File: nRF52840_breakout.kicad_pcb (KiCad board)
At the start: 4 copper layers, 24.1 x 34.3 mm, 66 parts, among them J2 Conn_ARM_JTAG_SWD_10, J3 Conn_01x22, J4 Conn_01x16, J5 Conn_01x22, J6 S2B-PH-SM4-TB(LF)(SN), J7 Conn_Coaxial, U1 nRF52840, U2 BQ24072, U3 TPS63031, U4 BME680, U5 MM8130-2600RA2, Y1 SiT1533, Y2 32MHz-XRCGB32M000F1H00R0

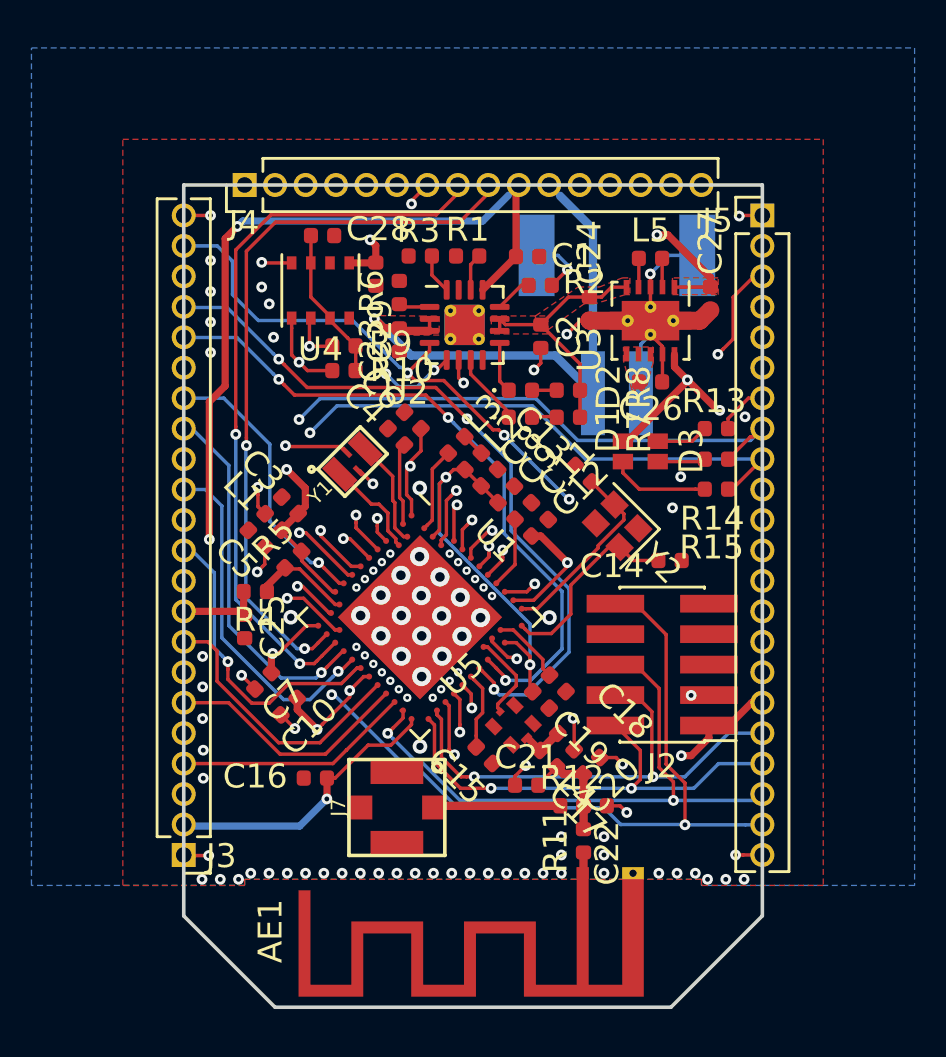
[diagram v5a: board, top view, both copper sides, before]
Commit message: 2 layer som version
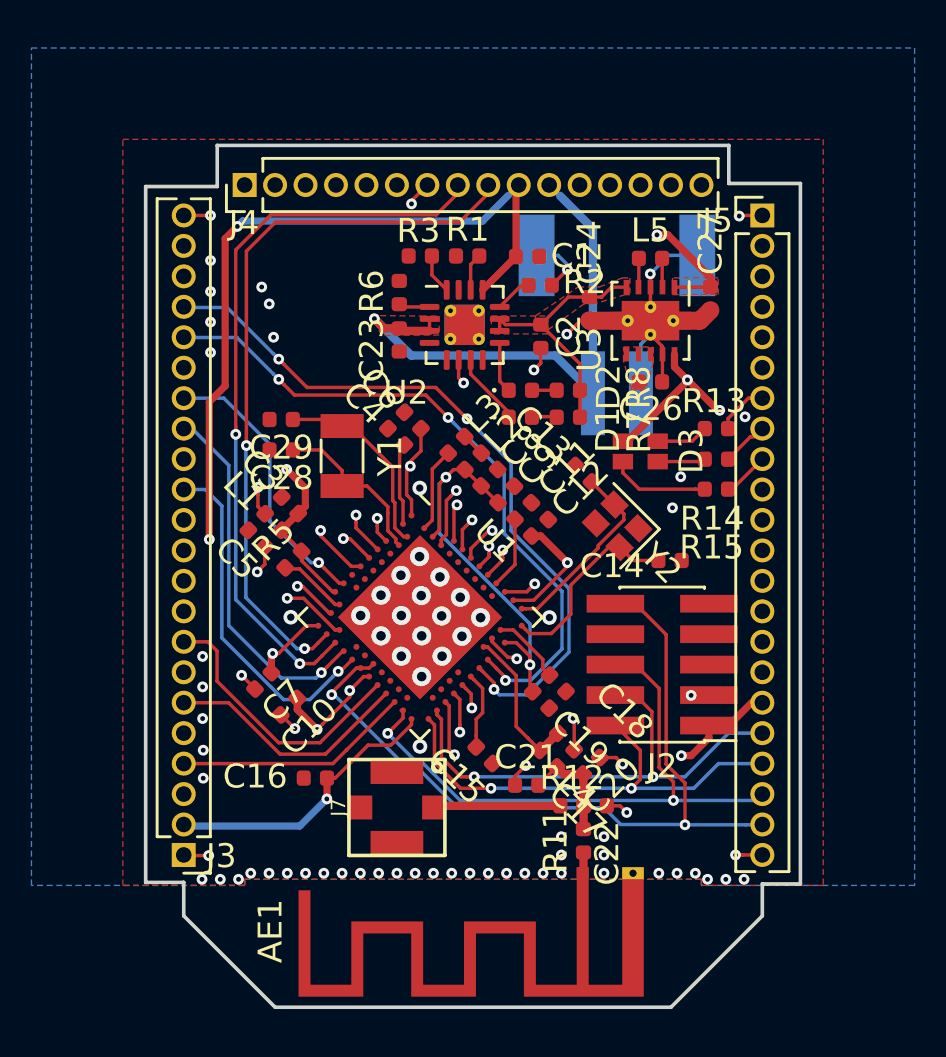
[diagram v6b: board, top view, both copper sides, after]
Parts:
- removed C25: NC, Capacitor_SMD:C_0402_1005Metric
- removed R10, R9: 4.7k, Resistor_SMD:R_0402_1005Metric
- removed R4: NC, Resistor_SMD:R_0402_1005Metric
- removed U4: BME680, Package_LGA:Bosch_LGA-8_3x3mm_P0.8mm_ClockwisePinNumbering
- removed U5: MM8130-2600RA2, custom_footprints:MM8930_2620
- AE1: value Antenna_Shield -> TI_SWRA117D
- C28, C29: value 100nF -> 12.5pF
- J7: value Conn_Coaxial -> U.FL_A-1JB
- L1: value NC -> 10uF
- R13, R14, R15: value 1.5k -> 180R
- Y1: value SiT1533 -> 32.768kHz; footprint custom_footprints:Crystal_SMD_2012-4Pin_2.2mmx1.4mm -> Crystal:Crystal_SMD_3215-2Pin_3.2x1.5mm
- moved C28 9.10 mm to (103.1, 64.4)
- moved C29 7.23 mm to (103.1, 63.1), turned to 180 degrees
- moved Y1 0.49 mm to (105.7, 64.6), turned to 270 degrees
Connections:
- C28 pad 1: GND -> Net-(C28-Pad1)
- C28 pad 2: VDDIO -> GND
- C29 pad 1: GND -> Net-(C29-Pad1)
- C29 pad 2: VDD_nRF -> GND
- J3 pad 10: P0.19 -> Net-(J3-Pad10)
- J3 pad 11: P0.17 -> Net-(J3-Pad11)
- J3 pad 12: P0.16 -> Net-(J3-Pad12)
- J3 pad 14: P0.14 -> Net-(J3-Pad14)
- J3 pad 17: P0.11 -> Net-(J3-Pad17)
- J3 pad 21: P0.03_AIN1 -> Net-(J3-Pad21)
- J3 pad 3: P0.25 -> Net-(J3-Pad3)
- J3 pad 5: P0.23 -> Net-(J3-Pad5)
- J3 pad 7: P0.21 -> Net-(J3-Pad7)
- J3 pad 9: VDDH -> Net-(J3-Pad9)
- J4 pad 1: P0.07 -> Net-(J4-Pad1)
- J4 pad 13: P0.30_AIN6 -> Net-(J4-Pad13)
- J4 pad 15: P0.28_AIN4 -> Net-(J4-Pad15)
- J4 pad 3: P0.05_AIN3 -> Net-(J4-Pad3)
- J4 pad 5: P0.27 -> Net-(J4-Pad5)
- J5 pad 10: P1.07 -> Net-(J5-Pad10)
- J5 pad 12: P1.05 -> Net-(J5-Pad12)
- J5 pad 14: P1.03 -> Net-(J5-Pad14)
- J5 pad 16: P1.01 -> Net-(J5-Pad16)
- J5 pad 3: P1.14 -> Net-(J5-Pad3)
- J5 pad 5: P1.12 -> Net-(J5-Pad5)
- J5 pad 6: P1.11 -> Net-(J5-Pad6)
- J5 pad 9: P1.08 -> Net-(J5-Pad9)
- U1 pad AC11: P0.16 -> Net-(U1-PadAC11)
- U1 pad AC15: P0.19 -> Net-(U1-PadAC15)
- U1 pad AC17: P0.21 -> Net-(U1-PadAC17)
- U1 pad AC19: P0.23 -> Net-(U1-PadAC19)
- U1 pad AC21: P0.25 -> Net-(U1-PadAC21)
- U1 pad AC9: P0.14 -> Net-(U1-PadAC9)
- U1 pad AD12: P0.17 -> P1.18_RESET
- U1 pad B11: P0.28_AIN4 -> Net-(U1-PadB11)
- U1 pad B13: P0.03_AIN1 -> Net-(U1-PadB13)
- U1 pad B15: P1.14 -> Net-(U1-PadB15)
- U1 pad B17: P1.12 -> Net-(U1-PadB17)
- U1 pad B19: P1.11 -> Net-(U1-PadB19)
- U1 pad B9: P0.30_AIN6 -> Net-(U1-PadB9)
- U1 pad D2: Net-(U1-PadD2) -> Net-(C29-Pad1)
- U1 pad F2: Net-(U1-PadF2) -> Net-(C28-Pad1)
- U1 pad H2: P0.27 -> Net-(U1-PadH2)
- U1 pad H23: Net-(U1-PadH23) -> Net-(C17-Pad2)
- U1 pad K2: P0.05_AIN3 -> Net-(U1-PadK2)
- U1 pad M2: P0.07 -> Net-(U1-PadM2)
- U1 pad P2: P1.08 -> Net-(U1-PadP2)
- U1 pad P23: P1.07 -> Net-(U1-PadP23)
- U1 pad T2: P0.11 -> Net-(U1-PadT2)
- U1 pad T23: P1.05 -> Net-(U1-PadT23)
- U1 pad V23: P1.03 -> Net-(U1-PadV23)
- U1 pad Y23: P1.01 -> Net-(U1-PadY23)
- Y1 pad 1: Net-(U1-PadF2) -> Net-(C28-Pad1)
- Y1 pad 2: GND -> Net-(C29-Pad1)
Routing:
- net P1.09: track 35.1 -> 1.47 mm, vias 3 -> 0
- net P1.08: track 34.5 -> 1.48 mm, vias 3 -> 0
- net P0.03_AIN1: track 28.2 -> 0.00 mm, vias 4 -> 0
- net P0.28_AIN4: track 19.7 -> 0.00 mm, vias 1 -> 0
- net P0.27: track 19.3 -> 0.00 mm, vias 3 -> 0
- net P0.07: track 18.3 -> 0.00 mm, vias 1 -> 0
- net P1.14: track 18.2 -> 0.00 mm, vias 2 -> 0
- net P0.30_AIN6: track 17.8 -> 0.00 mm, vias 1 -> 0
- net P1.01: track 17.8 -> 0.00 mm, vias 1 -> 0
- net P1.05: track 17.4 -> 0.00 mm, vias 1 -> 0
- net P1.03: track 17.3 -> 0.00 mm, vias 1 -> 0
- net P0.05_AIN3: track 16.7 -> 0.00 mm, vias 1 -> 0
- net P1.07: track 16.5 -> 0.00 mm, vias 1 -> 0
- net P1.12: track 15.7 -> 0.00 mm, vias 1 -> 0
- net P1.11: track 14.9 -> 0.00 mm, vias 1 -> 0
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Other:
- board size 24.1 x 34.3 mm -> 27.3 x 35.9 mm

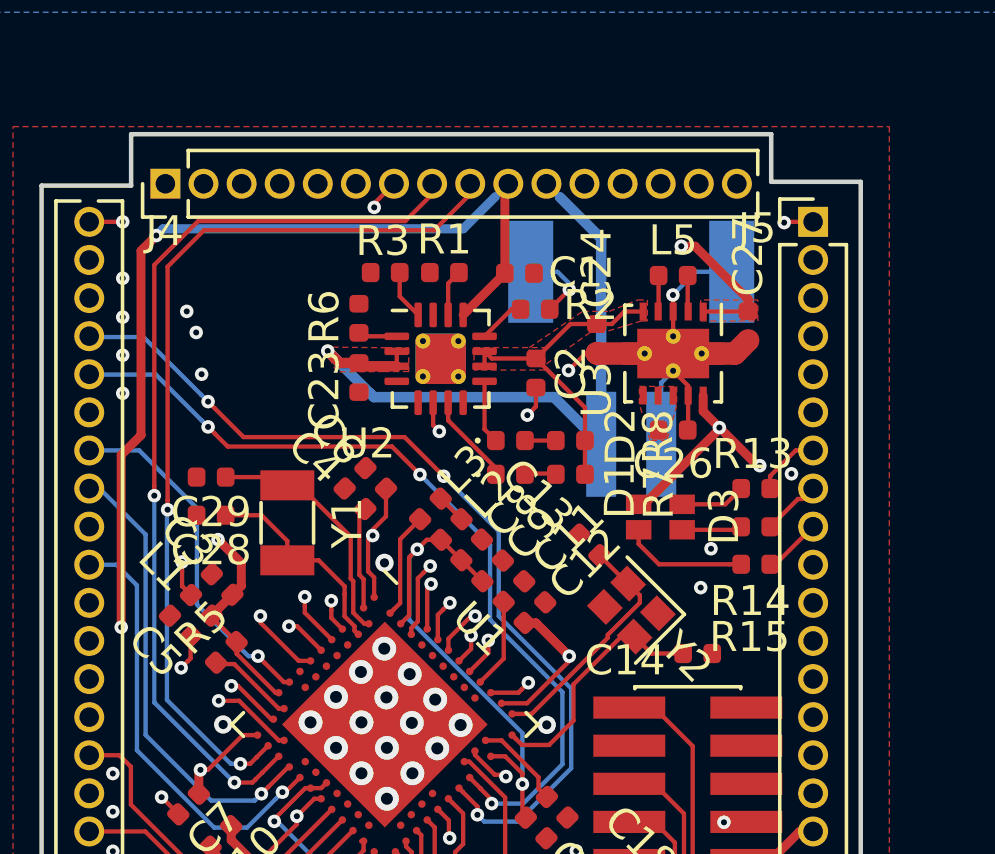
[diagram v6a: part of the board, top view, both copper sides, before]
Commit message: different power path management / got rid of var components
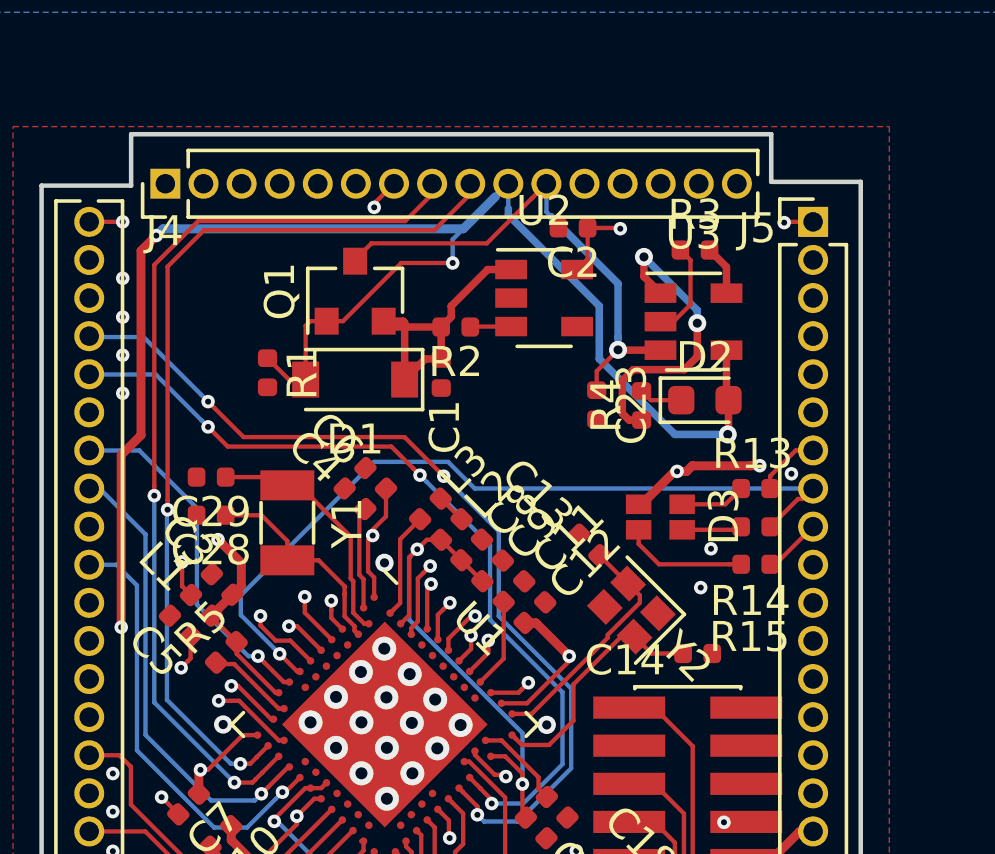
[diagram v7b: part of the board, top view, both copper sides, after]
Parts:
- removed C24, C27: 10µF, Capacitor_SMD:C_0402_1005Metric
- removed C26: 0.1µF, Capacitor_SMD:C_0402_1005Metric
- removed J6: S2B-PH-SM4-TB(LF)(SN), custom_footprints:JST_PH_S2B-PH-SM4-TB_LF__SN_
- removed L5: 1.5µH, Inductor_SMD:L_0402_1005Metric
- removed R6: 10k, Resistor_SMD:R_0402_1005Metric
- removed R7, R8: 1.5k, Resistor_SMD:R_0402_1005Metric
- added Q1: NTR1P02T1GOSTR-ND, Package_TO_SOT_SMD:SOT-23, F.Cu at (107.9, 56.9)
- added R4: 1k, Resistor_SMD:R_0402_1005Metric, F.Cu at (117.5, 60.7)
- C1, C2, C23: value 10µF -> 10uF
- D1: value GRN -> MBR120; footprint LED_SMD:LED_0402_1005Metric -> Diode_SMD:D_SOD-123
- D2: value RED -> LED_ORG; footprint LED_SMD:LED_0402_1005Metric -> LED_SMD:LED_0603_1608Metric
- R1: value 46.4k -> 100k
- R2: value 1.18k -> 100k
- R3: value 1.13k -> 2k
- U2: value BQ24072 -> AP2112K-3.3; footprint Package_DFN_QFN:VQFN-16-1EP_3x3mm_P0.5mm_EP1.68x1.68mm_ThermalVias -> Package_TO_SOT_SMD:SOT-23-5
- U3: value TPS63031 -> MCP73831-2-OT; footprint Package_SON:Texas_DRC0010J_ThermalVias -> Package_TO_SOT_SMD:SOT-23-5
- moved R3 10.4 mm to (119.3, 55.5), turned to 0 degrees
- moved C23 7.98 mm to (116.0, 60.7)
- moved R1 6.78 mm to (105.0, 59.6), turned to 270 degrees
- moved D2 6.62 mm to (119.6, 60.6)
- moved D1 6.06 mm to (107.9, 59.9), turned to 180 degrees
- moved C2 4.99 mm to (115.2, 54.8), turned to 180 degrees
- moved C1 4.24 mm to (110.8, 59.7), turned to 270 degrees
- moved U2 4.00 mm to (114.2, 57.1)
- moved R2 2.71 mm to (111.3, 58.1), turned to 180 degrees
- moved U3 1.26 mm to (119.2, 57.9), turned to 0 degrees
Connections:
- net P0.03_AIN1 renamed Net-(U2-Pad4)
- C1 pad 1: VBUS_nRF -> Net-(C1-Pad1)
- C2 pad 1: V_SYS -> VDD_nRF
- D1 pad 1: Net-(D1-Pad1) -> Net-(C1-Pad1)
- D1 pad 2: Net-(D1-Pad2) -> VBUS_nRF
- D2 pad 2: Net-(D2-Pad2) -> VBUS_nRF
- R1 pad 1: Net-(R1-Pad1) -> VBUS_nRF
- R2 pad 2: GND -> Net-(C1-Pad1)
- R3 pad 2: GND -> Net-(R3-Pad2)
- U2 pad 1: Net-(R6-Pad2) -> Net-(C1-Pad1)
- U2 pad 2: VDD_BAT -> GND
- U2 pad 3: VDD_BAT -> Net-(R2-Pad1)
- U2 pad 5: P0.27 -> VDD_nRF
- U3 pad 1: VDD_nRF -> Net-(R4-Pad1)
- U3 pad 2: Net-(L5-Pad2) -> Net-(R3-Pad1)
- U3 pad 3: GND -> VDD_BAT
- U3 pad 4: Net-(L5-Pad1) -> VBUS_nRF
- U3 pad 5: V_SYS -> Net-(R3-Pad2)
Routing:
- net P1.09: track 1.47 -> 26.2 mm, vias 0 -> 1
- net VBUS_nRF: track 39.1 -> 62.3 mm, vias 3 -> 5
- net GND: track 30.0 -> 13.4 mm, vias 82 -> 77
- net V_SYS: track 11.1 -> 0.00 mm
- net Net-(C1-Pad1): track 0.00 -> 10.5 mm
- net Net-(R4-Pad1): track 0.00 -> 10.2 mm, vias 0 -> 2
- net VDD_nRF: track 54.6 -> 48.6 mm, vias 13 -> 11
- net VDD_BAT: track 22.2 -> 17.1 mm
- net P0.26: track 20.0 -> 15.0 mm, vias 2 -> 1
- net Net-(D1-Pad1): track 3.02 -> 0.00 mm
- net Net-(R3-Pad2): track 0.00 -> 1.67 mm
- net Net-(R1-Pad1): track 1.56 -> 0.00 mm
- net Net-(R3-Pad1): track 1.67 -> 3.19 mm
- net Net-(R6-Pad2): track 1.31 -> 0.00 mm
- net Net-(L5-Pad2): track 1.21 -> 0.00 mm
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- removed copper zone on F.Cu, net Net-(C26-Pad1)
- removed copper zone on F.Cu, net VDD_BAT
- removed copper zone on F.Cu, net VDD_nRF
- removed copper zone on F.Cu, net V_SYS

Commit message: modified bom / fixed silk,fab / added 3D models
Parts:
- removed R13, R14, R15: 180R, Resistor_SMD:R_0402_1005Metric
- added R6: 68R, Resistor_SMD:R_0402_1005Metric, F.Cu at (117.1, 63.3)
- C13, C14: value 6pF -> 8pF
- C28, C29: value 12.5pF -> 7pF
- C3, C5, C7: value 4.7µF -> 4.7uF
- C6, C8: value 1µF -> 1uF
- D3: value LTST-C19HE1WT -> LED_RED; footprint custom_footprints:LTST-C19HE1WT -> LED_SMD:LED_0603_1608Metric
- L1: value 10uF -> 10uH; footprint Inductor_SMD:L_0402_1005Metric -> Inductor_SMD:L_0603_1608Metric
- L3: value 10µH -> 10uH; footprint Inductor_SMD:L_0402_1005Metric -> Inductor_SMD:L_0603_1608Metric
- Q1: value NTR1P02T1GOSTR-ND -> pmos
- Y1: footprint Crystal:Crystal_SMD_3215-2Pin_3.2x1.5mm -> custom_footprints:Crystal_SMD_2012-2Pin_2.0x1.2mm
- Y2: value 32MHz-XRCGB32M000F1H00R0 -> 32MHz; footprint Crystal:Crystal_SMD_2016-4Pin_2.0x1.6mm -> custom_footprints:Crystal_SMD_2016-4Pin_2.0x1.6mm
- moved D3 2.39 mm to (119.6, 63.3), turned to 180 degrees
- moved C5 0.57 mm to (101.7, 68.5)
- moved L3 0.55 mm to (110.7, 63.7)
- moved L1 0.43 mm to (102.4, 67.4)
- moved C13 0.37 mm to (116.0, 65.2)
- turned Y1 to 90 degrees
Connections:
- D3 pad 1: Net-(D3-Pad1) -> GND
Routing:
- net VDD_nRF: track 48.6 -> 40.9 mm, vias 11 -> 9
- net Net-(D3-Pad3): track 4.17 -> 0.00 mm
- net Net-(D3-Pad1): track 2.18 -> 0.00 mm
- net P1.10: track 15.7 -> 13.8 mm
- net P1.08: track 1.48 -> 0.00 mm
- net Net-(C17-Pad2): track 6.43 -> 7.62 mm
- net GND: track 13.4 -> 14.4 mm, vias 77 -> 83
- net Net-(D3-Pad2): track 2.01 -> 1.29 mm
- net P1.09: track 26.2 -> 25.5 mm
- net Net-(L1-Pad2): track 7.90 -> 8.52 mm
- net Net-(L2-Pad2): track 0.98 -> 1.57 mm
- added copper zone on F.Cu, net Net-(C1-Pad1)
- added copper zone on F.Cu, net VBUS_nRF
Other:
- outline, holes or cut-outs redrawn
